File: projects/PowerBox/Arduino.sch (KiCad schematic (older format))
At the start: 63 parts, among them CON3 USB-MINI-B-Vert, IC3 LM358, P10 CONN_4, P11 CONN_10, P12 CONN_8, P13 CONN_8, P14 CONN_6, P15 CONN_4, P7 CONN_3X2, P8 CONN_4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

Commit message: basic part placement
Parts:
- P10: value CONN_4 -> Analog
- P15: value CONN_4 -> Digital
- P8: value CONN_4 -> Serial
- P9: value CONN_4 -> I2C
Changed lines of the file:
@@
 P 8900 6100
 F 0 "P9" V 8850 6100 50  0000 C CNN
-F 1 "CONN_4" V 8950 6100 50  0000 C CNN
+F 1 "I2C" V 8950 6100 50  0000 C CNN
 F 2 "frep:grove_con_straight" H 8900 6100 60  0001 C CNN
 F 3 "" H 8900 6100 60  0000 C CNN
@@
 P 9850 6100
 F 0 "P10" V 9800 6100 50  0000 C CNN
-F 1 "CONN_4" V 9900 6100 50  0000 C CNN
+F 1 "Analog" V 9900 6100 50  0000 C CNN
 F 2 "frep:grove_con_straight" H 9850 6100 60  0001 C CNN
 F 3 "" H 9850 6100 60  0000 C CNN
@@
 P 8000 6100
 F 0 "P8" V 7950 6100 50  0000 C CNN
-F 1 "CONN_4" V 8050 6100 50  0000 C CNN
+F 1 "Serial" V 8050 6100 50  0000 C CNN
 F 2 "frep:grove_con_straight" H 8000 6100 60  0001 C CNN
 F 3 "" H 8000 6100 60  0000 C CNN
@@
 P 10800 6100
 F 0 "P15" V 10750 6100 50  0000 C CNN
-F 1 "CONN_4" V 10850 6100 50  0000 C CNN
+F 1 "Digital" V 10850 6100 50  0000 C CNN
 F 2 "frep:grove_con_straight" H 10800 6100 60  0001 C CNN
 F 3 "" H 10800 6100 60  0000 C CNN

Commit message: layout in progress
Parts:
- removed P10: Analog, frep:grove_con_straight, symbol CONN_4
- removed P15: Digital, frep:grove_con_straight, symbol CONN_4
- removed P8: Serial, frep:grove_con_straight, symbol CONN_4
- removed P9: I2C, frep:grove_con_straight, symbol CONN_4
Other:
- note removed: "Grove headers"
- moved on the sheet: JP4, JP5, P7, R24, R25, R28, R36, S5, U4

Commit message: layout in progress
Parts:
- D15: value Power -> Power Ard.
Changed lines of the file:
@@
 Rev "A"
 Comp ""
-Comment1 " - Grove connectors (1xI2C, 1xDigital, 1xAnalog, 1xSerial)"
+Comment1 ""
 Comment2 " - 4 Neopixel"
 Comment3 " - INA219 (over I2C)"
@@
 P 5500 7200
 F 0 "D15" H 5500 7300 50  0000 C CNN
-F 1 "Power" H 5500 7100 50  0000 C CNN
+F 1 "Power Ard." H 5500 7100 50  0000 C CNN
 F 2 "frep:LED-0805" H 5500 7200 60  0001 C CNN
 F 3 "" H 5500 7200 60  0000 C CNN
@@
 	1    0    0    -1
 $EndComp
-Text GLabel 8700 6000 2    47   Input ~ 0
-D7
 Text GLabel 8700 5700 2    47   Input ~ 0
 D5
@@
 Wire Bus Line
 	900  1000 3900 1000
+Text GLabel 8700 6000 2    47   Input ~ 0
+IO_10
 $EndSCHEMATC

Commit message: layout in progress
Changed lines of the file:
@@
 	1    0    0    -1
 $EndComp
-Text GLabel 8700 5700 2    47   Input ~ 0
-D5
-Text GLabel 8700 5850 2    47   Input ~ 0
-D6
 Connection ~ 2650 4150
 $Comp
@@
 Wire Bus Line
 	900  1000 3900 1000
+Text GLabel 8700 5700 2    47   Input ~ 0
+IO_12
+Text GLabel 8700 5850 2    47   Input ~ 0
+D7
 Text GLabel 8700 6000 2    47   Input ~ 0
-IO_10
+IO_11
 $EndSCHEMATC

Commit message: pcb layout most traces done
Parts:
- removed C13, C14, C15, C17: 100nF, frep:C0805, symbol C
- removed JP3: JUMPER, frep:Pin_Proto_Straight_1x02, symbol JUMPER
- removed N1, N2, N3, N4: Neopixel, frep:Neopixel, symbol Neopixel
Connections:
- no-connect marks 8 -> 3
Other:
- note removed: "Neopixel"

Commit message: pcb still not finished
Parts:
- P7: value CONN_3X2 -> ICSP
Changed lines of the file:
@@
 P 9975 5950
 F 0 "P7" H 9975 6200 50  0000 C CNN
-F 1 "CONN_3X2" V 9975 6000 40  0000 C CNN
+F 1 "ICSP" V 9975 6000 40  0000 C CNN
 F 2 "frep:Pin_Proto_Straight_2x03" H 9975 5950 60  0001 C CNN
 F 3 "" H 9975 5950 60  0000 C CNN

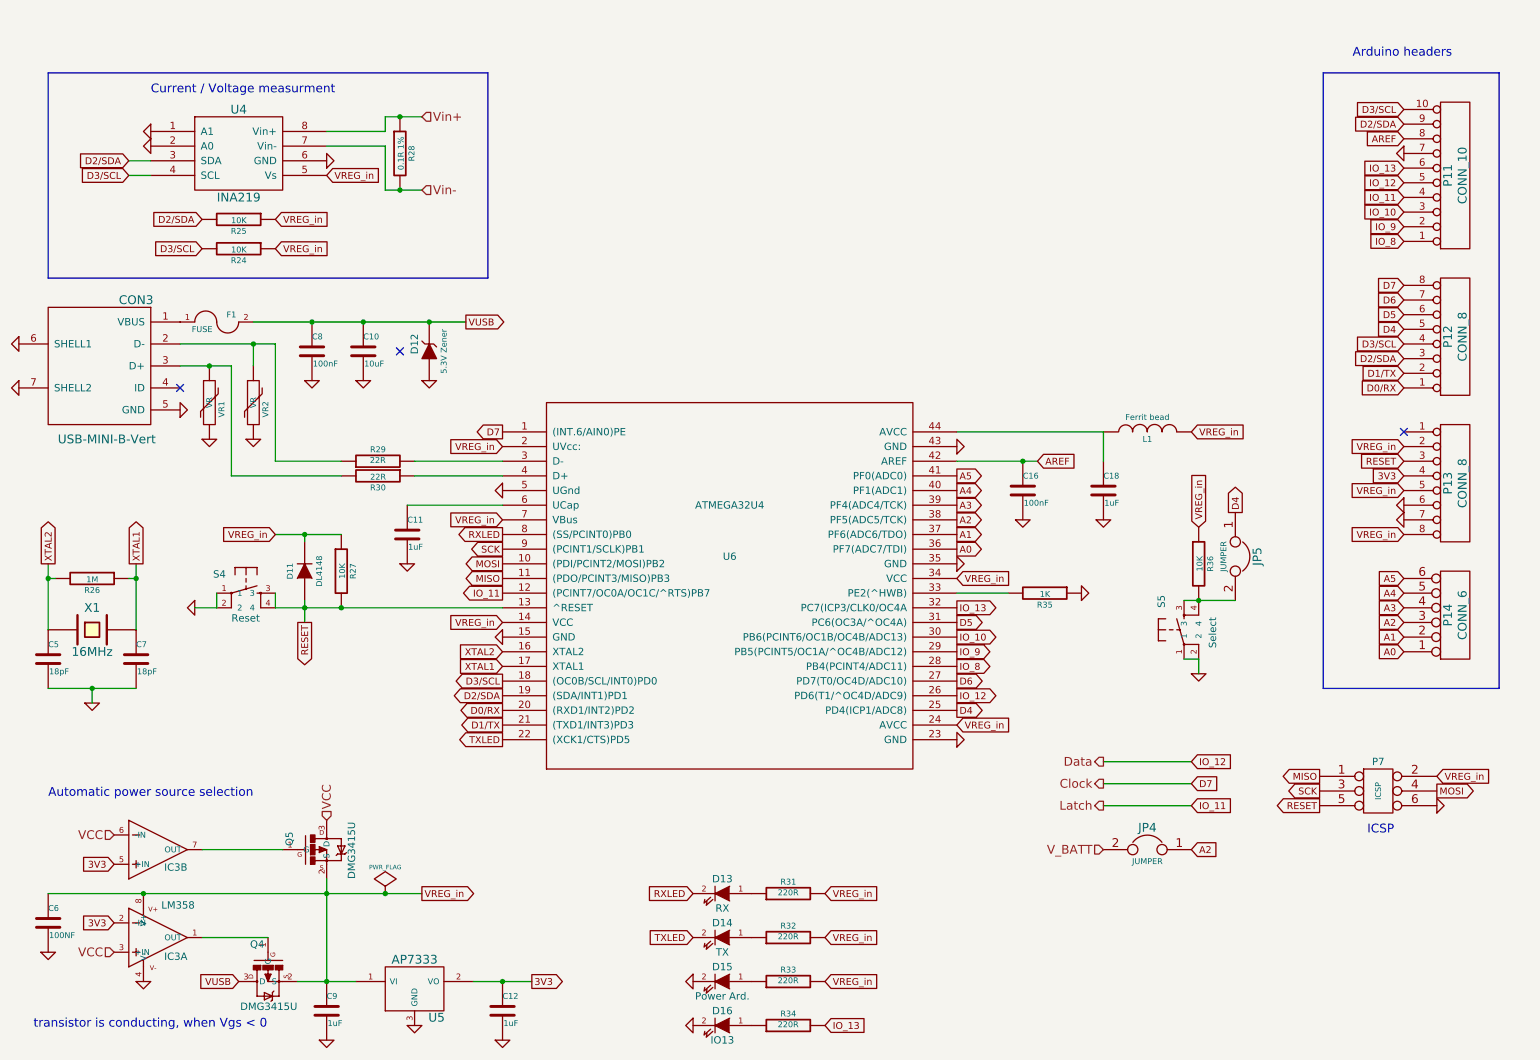
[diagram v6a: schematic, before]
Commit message: start changing power lines
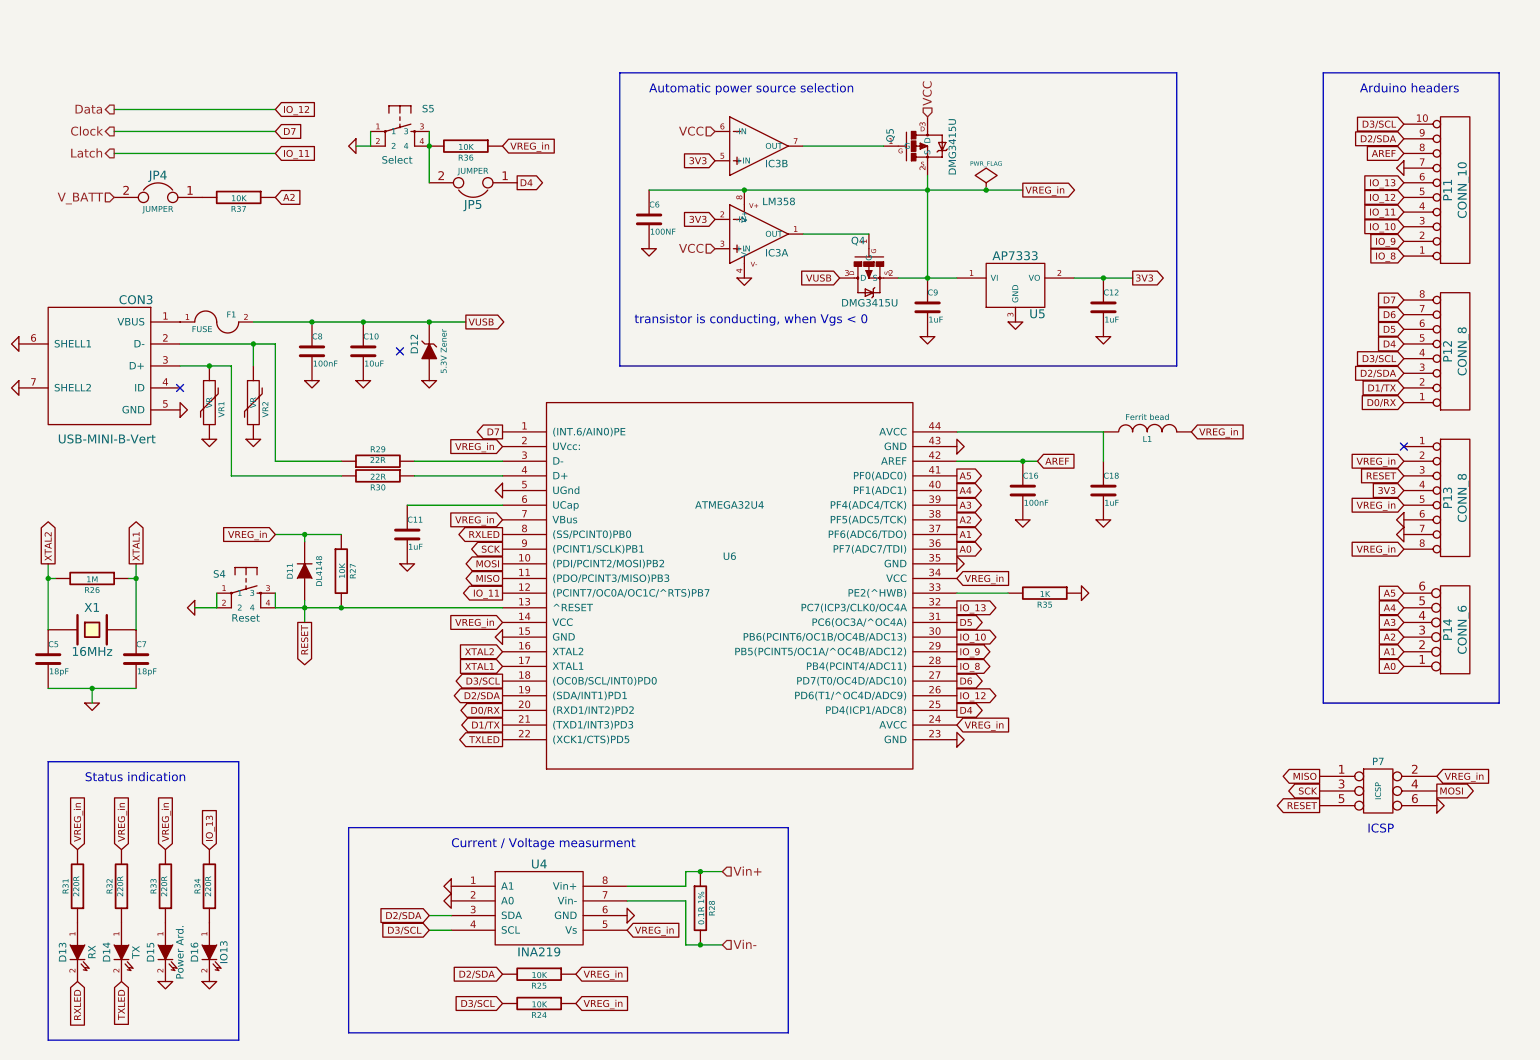
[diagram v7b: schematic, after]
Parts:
- added R37: 10K, frep:R0805, symbol R
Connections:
- net A2: now also R37.1; no longer JP4.1
- new net: JP4.1, R37.2
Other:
- note added: "Status indication"
- moved on the sheet: C12, C6, C9, D13, D14, D15, D16, IC3A, IC3B, JP4, JP5, P11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

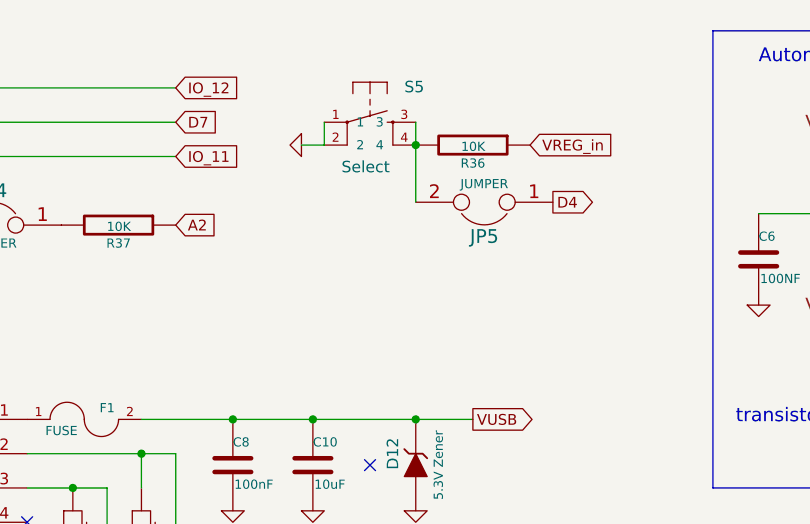
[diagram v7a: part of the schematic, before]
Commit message: arduino pins labled
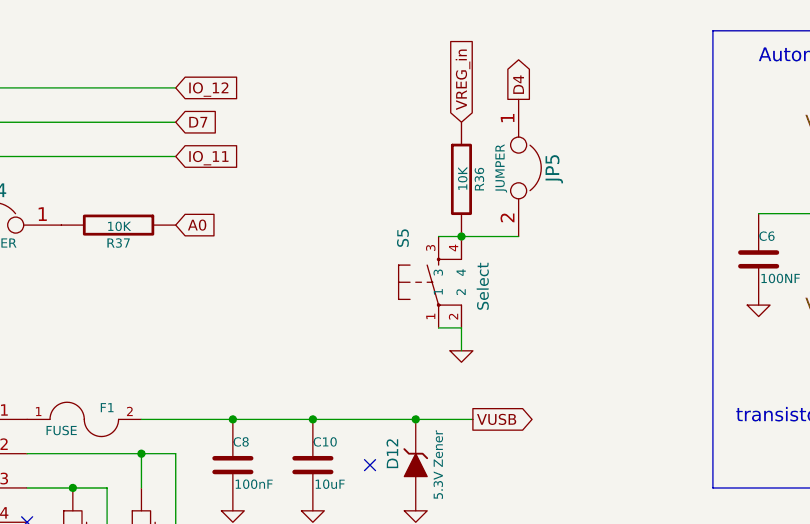
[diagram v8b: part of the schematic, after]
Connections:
- net A0: now also R37.1
- net A2: no longer R37.1
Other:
- moved on the sheet: JP5, R36, S5
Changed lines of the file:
@@
 L TAC_SWITCH S5
 U 1 1 558D6CB3
-P 3300 1400
-F 0 "S5" H 3450 1525 50  0000 L BNN
-F 1 "Select" H 3175 1175 50  0000 L BNN
-F 2 "frep:TACTILE-PTH" H 3300 1550 50  0001 C CNN
-F 3 "" H 3300 1400 60  0000 C CNN
-	1    3300 1400
-	1    0    0    -1
+P 3600 2100
+F 0 "S5" H 3750 2225 50  0000 L BNN
+F 1 "Select" H 3475 1875 50  0000 L BNN
+F 2 "frep:TACTILE-PTH" H 3600 2250 50  0001 C CNN
+F 3 "" H 3600 2100 60  0000 C CNN
+	1    3600 2100
+	0    -1   -1   0
 $EndComp
 $Comp
 L R R36
 U 1 1 558D6CC5
-P 3750 1500
-F 0 "R36" V 3830 1500 40  0000 C CNN
-F 1 "10K" V 3757 1501 40  0000 C CNN
-F 2 "frep:R0805" V 3680 1500 30  0001 C CNN
-F 3 "" H 3750 1500 30  0000 C CNN
-	1    3750 1500
-	0    1    1    0
-$EndComp
-Text GLabel 4100 1750 2    47   Output ~ 0
+P 3700 1650
+F 0 "R36" V 3780 1650 40  0000 C CNN
+F 1 "10K" V 3707 1651 40  0000 C CNN
+F 2 "frep:R0805" V 3630 1650 30  0001 C CNN
+F 3 "" H 3700 1650 30  0000 C CNN
+	1    3700 1650
+	1    0    0    -1
+$EndComp
+Text GLabel 3950 1300 1    47   Output ~ 0
 D4
 $Comp
 L GND #PWR063
 U 1 1 558D6D6B
-P 3000 1500
-F 0 "#PWR063" H 3000 1500 30  0001 C CNN
-F 1 "GND" H 3000 1430 30  0001 C CNN
-F 2 "" H 3000 1500 60  0000 C CNN
-F 3 "" H 3000 1500 60  0000 C CNN
-	1    3000 1500
-	0    1    1    0
+P 3700 2400
+F 0 "#PWR063" H 3700 2400 30  0001 C CNN
+F 1 "GND" H 3700 2330 30  0001 C CNN
+F 2 "" H 3700 2400 60  0000 C CNN
+F 3 "" H 3700 2400 60  0000 C CNN
+	1    3700 2400
+	1    0    0    -1
 $EndComp
 $Comp
@@
 Text GLabel 10375 5800 2    47   Input ~ 0
 VREG_in
-Text GLabel 4000 1500 2    47   Input ~ 0
+Text GLabel 3700 1400 1    47   Input ~ 0
 VREG_in
 Text GLabel 1100 6300 1    47   Input ~ 0
@@
 Text GLabel 4500 7150 2    47   Input ~ 0
 VREG_in
-Wire Wire Line
-	900  5200 1500 5200
-Wire Wire Line
-	1500 4350 1500 4800
-Wire Wire Line
-	1200 5300 1200 5200
-Connection ~ 1200 5200
-Wire Wire Line
-	4000 3950 3350 3950
-Wire Wire Line
-	950  4450 900  4450
-Connection ~ 1500 4450
-Connection ~ 900  4450
-Wire Wire Line
-	2450 4150 2900 4150
-Wire Wire Line
-	2650 4150 2650 4200
-Wire Wire Line
-	2450 4650 4000 4650
-Connection ~ 2900 4650
-Wire Wire Line
-	2450 4650 2450 4550
-Wire Wire Line
-	2050 4550 2050 4650
-Wire Wire Line
-	2050 4650 1900 4650
-Wire Wire Line
-	2650 4600 2650 4750
-Connection ~ 2650 4650
-Wire Wire Line
-	7100 3650 7650 3650
-Wire Wire Line
-	7100 3450 8100 3450
-Wire Wire Line
-	7450 4550 7100 4550
-Wire Wire Line
-	3500 1400 3500 1750
-Wire Wire Line
-	3100 1400 3100 1500
-Wire Wire Line
-	3100 1500 3000 1500
-Wire Wire Line
-	2300 2700 3750 2700
-Connection ~ 2700 2700
-Connection ~ 3050 2700
-Connection ~ 7550 3650
-Wire Wire Line
-	8100 3450 8100 3650
-Wire Wire Line
-	6050 2100 6500 2100
-Connection ~ 5650 1800
-Wire Wire Line
-	6700 2400 7100 2400
-Connection ~ 6900 2400
-Connection ~ 6900 1800
-Wire Wire Line
-	7900 2400 8300 2400
-Connection ~ 8100 2400
 Text HLabel 5500 6450 2    60   Input ~ 0
 Vin+
@@
 	1    0    0    -1
 $EndComp
-Connection ~ 2650 4150
 $Comp
 L JUMPER JP5
 U 1 1 558E93BB
-P 3800 1750
-F 0 "JP5" H 3800 1900 60  0000 C CNN
-F 1 "JUMPER" H 3800 1670 40  0000 C CNN
-F 2 "frep:Pin_Proto_Straight_1x02" H 3800 1750 60  0001 C CNN
-F 3 "" H 3800 1750 60  0000 C CNN
-	1    3800 1750
-	-1   0    0    1
-$EndComp
-Connection ~ 3500 1500
+P 3950 1600
+F 0 "JP5" H 3950 1750 60  0000 C CNN
+F 1 "JUMPER" H 3950 1520 40  0000 C CNN
+F 2 "frep:Pin_Proto_Straight_1x02" H 3950 1600 60  0001 C CNN
+F 3 "" H 3950 1600 60  0000 C CNN
+	1    3950 1600
+	0    1    1    0
+$EndComp
 $Comp
 L JUMPER JP4
@@
 	-1   0    0    -1
 $EndComp
-Text GLabel 2450 1850 2    47   Input ~ 0
-A2
 Text GLabel 4000 7350 0    47   Input ~ 0
 D3/SCL
@@
 Text HLabel 1350 1550 0    60   Output ~ 0
 Latch
-Wire Wire Line
-	1350 1250 2450 1250
-Wire Wire Line
-	1350 1400 2450 1400
-Wire Wire Line
-	1350 1550 2450 1550
 $Comp
 L INA219 U4
@@
 Text GLabel 4000 5050 0    47   Input ~ 0
 XTAL1
-Wire Wire Line
-	1450 4450 1500 4450
 Text GLabel 900  4350 1    47   Output ~ 0
 XTAL2
 Text GLabel 1500 4350 1    47   Output ~ 0
 XTAL1
-Wire Wire Line
-	900  4350 900  4800
 $Comp
 L MOSFET-P Q5
@@
 Text GLabel 5450 1600 0    47   Input ~ 0
 3V3
-Wire Wire Line
-	6900 1700 6900 2400
-Wire Wire Line
-	6050 1500 6600 1500
 $Comp
 L VR VR1
@@
 	1    0    0    -1
 $EndComp
-Wire Wire Line
-	4000 3650 3400 3650
-Wire Wire Line
-	1800 2850 2450 2850
-Wire Wire Line
-	1800 3000 2150 3000
-Wire Wire Line
-	3400 3750 4000 3750
 $Comp
 L PWR_FLAG #FLG079
@@
 	1    0    0    -1
 $EndComp
-Wire Wire Line
-	5000 1800 7550 1800
-Connection ~ 7300 1800
-Wire Wire Line
-	2450 2850 2450 3650
-Wire Wire Line
-	2450 3650 2900 3650
-Wire Wire Line
-	2300 3000 2300 2850
-Connection ~ 2300 2850
-Wire Wire Line
-	2900 3750 2150 3750
-Wire Wire Line
-	2150 3750 2150 3000
-Connection ~ 2000 3000
 $Comp
 L GND #PWR080
@@
 	1    0    0    -1
 $EndComp
-Connection ~ 3500 2700
 Text Notes 5000 1150 0    60   ~ 0
 Automatic power source selection
-Wire Bus Line
-	10800 5300 9600 5300
-Wire Bus Line
-	9600 5300 9600 1000
-Wire Bus Line
-	9600 1000 10800 1000
-Wire Bus Line
-	10800 1000 10800 5300
 Text Notes 9850 1150 0    60   ~ 0
 Arduino headers
@@
 Text Notes 3650 6300 0    60   ~ 0
 Current / Voltage measurment
-Wire Wire Line
-	3500 6750 3650 6750
-Wire Wire Line
-	3500 6850 3650 6850
-Wire Wire Line
-	5250 6950 5500 6950
-Wire Wire Line
-	5250 6950 5250 6650
-Wire Wire Line
-	5250 6650 4850 6650
-Connection ~ 5350 6950
-Wire Wire Line
-	5250 6450 5500 6450
-Wire Wire Line
-	4850 6550 5250 6550
-Wire Wire Line
-	5250 6550 5250 6450
-Connection ~ 5350 6450
 $Comp
 L ZENER_SOT23 D12
@@
 $EndComp
 NoConn ~ 3300 2900
-Wire Bus Line
-	5950 6150 5950 7550
-Wire Bus Line
-	5950 7550 2950 7550
-Wire Bus Line
-	2950 7550 2950 6150
-Wire Bus Line
-	2950 6150 5950 6150
 Text GLabel 2450 1250 2    47   Input ~ 0
 IO_12
@@
 Text GLabel 2450 1550 2    47   Input ~ 0
 IO_11
-Wire Bus Line
-	4800 1000 8600 1000
-Wire Bus Line
-	8600 1000 8600 3000
-Wire Bus Line
-	8600 3000 4800 3000
-Wire Bus Line
-	4800 3000 4800 1000
 Text Notes 1150 5850 0    60   ~ 0
 Status indication
-Wire Bus Line
-	900  5700 2200 5700
-Wire Bus Line
-	2200 5700 2200 7600
-Wire Bus Line
-	2200 7600 900  7600
-Wire Bus Line
-	900  7600 900  5700
 $Comp
 L R R37
@@
 	0    1    1    0
 $EndComp
+Wire Wire Line
+	900  5200 1500 5200
+Wire Wire Line
+	1500 4350 1500 4800
+Wire Wire Line
+	1200 5300 1200 5200
+Connection ~ 1200 5200
+Wire Wire Line
+	4000 3950 3350 3950
+Wire Wire Line
+	950  4450 900  4450
+Connection ~ 1500 4450
+Connection ~ 900  4450
+Wire Wire Line
+	2450 4150 2900 4150
+Wire Wire Line
+	2650 4150 2650 4200
+Wire Wire Line
+	2450 4650 4000 4650
+Connection ~ 2900 4650
+Wire Wire Line
+	2450 4650 2450 4550
+Wire Wire Line
+	2050 4550 2050 4650
+Wire Wire Line
+	2050 4650 1900 4650
+Wire Wire Line
+	2650 4600 2650 4750
+Connection ~ 2650 4650
+Wire Wire Line
+	7100 3650 7650 3650
+Wire Wire Line
+	7100 3450 8100 3450
+Wire Wire Line
+	7450 4550 7100 4550
+Wire Wire Line
+	3600 1900 3950 1900
+Wire Wire Line
+	3600 2300 3700 2300
+Wire Wire Line
+	3700 2300 3700 2400
+Wire Wire Line
+	2300 2700 3750 2700
+Connection ~ 2700 2700
+Connection ~ 3050 2700
+Connection ~ 7550 3650
+Wire Wire Line
+	8100 3450 8100 3650
+Wire Wire Line
+	6050 2100 6500 2100
+Connection ~ 5650 1800
+Wire Wire Line
+	6700 2400 7100 2400
+Connection ~ 6900 2400
+Connection ~ 6900 1800
+Wire Wire Line
+	7900 2400 8300 2400
+Connection ~ 8100 2400
+Connection ~ 2650 4150
+Connection ~ 3700 1900
+Wire Wire Line
+	1350 1250 2450 1250
+Wire Wire Line
+	1350 1400 2450 1400
+Wire Wire Line
+	1350 1550 2450 1550
+Wire Wire Line
+	1450 4450 1500 4450
+Wire Wire Line
+	900  4350 900  4800
+Wire Wire Line
+	6900 1700 6900 2400
+Wire Wire Line
+	6050 1500 6600 1500
+Wire Wire Line
+	4000 3650 3400 3650
+Wire Wire Line
+	1800 2850 2450 2850
+Wire Wire Line
+	1800 3000 2150 3000
+Wire Wire Line
+	3400 3750 4000 3750
+Wire Wire Line
+	5000 1800 7550 1800
+Connection ~ 7300 1800
+Wire Wire Line
+	2450 2850 2450 3650
+Wire Wire Line
+	2450 3650 2900 3650
+Wire Wire Line
+	2300 3000 2300 2850
+Connection ~ 2300 2850
+Wire Wire Line
+	2900 3750 2150 3750
+Wire Wire Line
+	2150 3750 2150 3000
+Connection ~ 2000 3000
+Connection ~ 3500 2700
+Wire Bus Line
+	10800 5300 9600 5300
+Wire Bus Line
+	9600 5300 9600 1000
+Wire Bus Line
+	9600 1000 10800 1000
+Wire Bus Line
+	10800 1000 10800 5300
+Wire Wire Line
+	3500 6750 3650 6750
+Wire Wire Line
+	3500 6850 3650 6850
+Wire Wire Line
+	5250 6950 5500 6950
+Wire Wire Line
+	5250 6950 5250 6650
+Wire Wire Line
+	5250 6650 4850 6650
+Connection ~ 5350 6950
+Wire Wire Line
+	5250 6450 5500 6450
+Wire Wire Line
+	4850 6550 5250 6550
+Wire Wire Line
+	5250 6550 5250 6450
+Connection ~ 5350 6450
+Wire Bus Line
+	5950 6150 5950 7550
+Wire Bus Line
+	5950 7550 2950 7550
+Wire Bus Line
+	2950 7550 2950 6150
+Wire Bus Line
+	2950 6150 5950 6150
+Wire Bus Line
+	4800 1000 8600 1000
+Wire Bus Line
+	8600 1000 8600 3000
+Wire Bus Line
+	8600 3000 4800 3000
+Wire Bus Line
+	4800 3000 4800 1000
+Wire Bus Line
+	900  5700 2200 5700
+Wire Bus Line
+	2200 5700 2200 7600
+Wire Bus Line
+	2200 7600 900  7600
+Wire Bus Line
+	900  7600 900  5700
+Text GLabel 2450 1850 2    47   Input ~ 0
+A0
 $EndSCHEMATC
